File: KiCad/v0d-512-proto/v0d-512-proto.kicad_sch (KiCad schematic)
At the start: 19 parts, among them U1 SST39SF040, U2 62256/628128, U3 74HC139, U4 74HC191, U5 74HC4520, U6 74HC191, U7 74HC191, U8 74HC670

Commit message: fix issues
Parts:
- added JP2, JP3, JP4, JP5: SolderJumper_2_Open, Jumper:SolderJumper-2_P1.3mm_Open_Pad1.0x1.5mm, symbol Jumper:SolderJumper_2_Open
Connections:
- net GND: no longer U6.5 (D/U), U7.5 (D/U)
- net VCC: now also JP1.3 (B), U6.5 (D/U), U7.5 (D/U)
- net pA11: now also JP2.2 (B)
- net pA12: now also JP3.2 (B)
- net pA13: now also JP4.2 (B), JP5.2 (B); no longer JP1.3 (B)
- net pBank0: now also JP2.1 (A)
- net pBank1: now also JP3.1 (A)
- net pBank2: now also JP4.1 (A)
- net pBank3: now also JP5.1 (A)
- net rfAUDIO: no longer names the net of H1.45 (cAUDIO), H1.46 (rfAUDIO)
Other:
- note added: "* 2048KiB PRG FLASH (rewrittable), 32KiB Window * 32KiB PRG RAM, 8KiB Window * 8KiB,32KiB,8KiB CHR RAM, 4x2KiB Window * Four-Screen Scrolling * Scanline IRQ"
- note added: ".... cccc"
- note added: ".... pppp"
- note added: "128K"
- note added: "32K"
- note added: "512K Through-Hole Proto"
- note added: "8K"
- note removed: "* 2048KiB PRG FLASH (rewrittable), 32KiB Window * 32KiB PRG RAM, 8KiB Window * 32KiB CHR RAM, 4x4KiB Window * Four-Screen Scrolling * Scanline IRQ"
- note removed: ".... bbbb"
- note removed: "is.. bbbb"
- moved on the sheet: H1, JP1, RN1, U1, U2, U3A, U3B, U4, U5A, U5B, U6, U7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

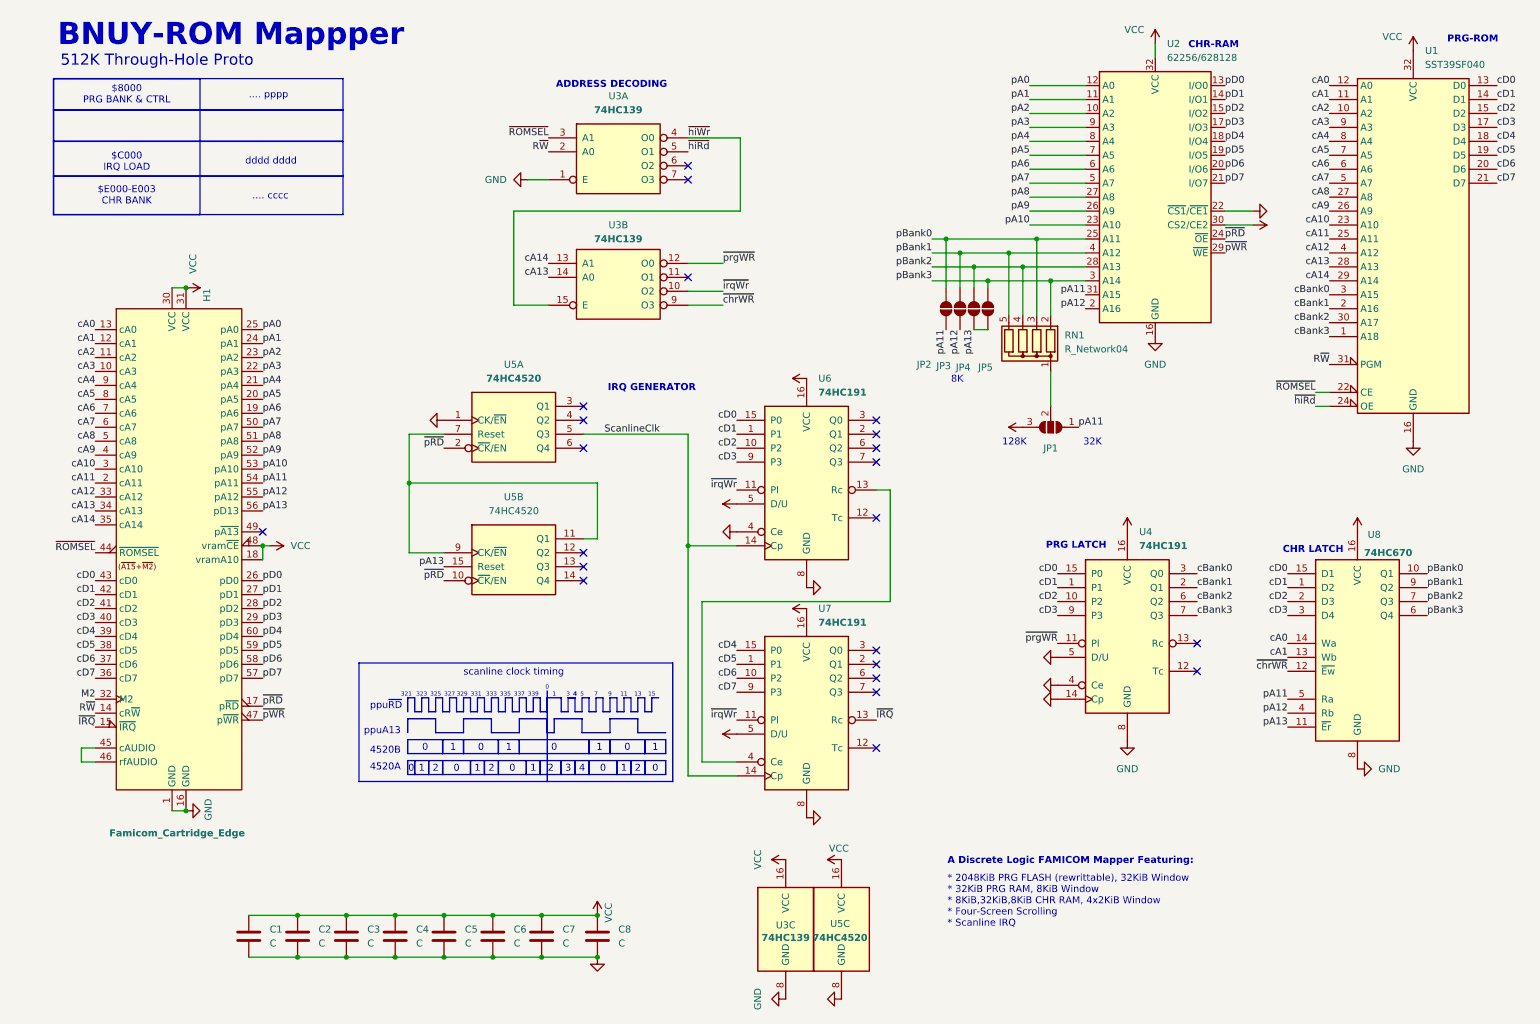
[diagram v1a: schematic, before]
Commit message: Update to latest pcb version, README tweaks
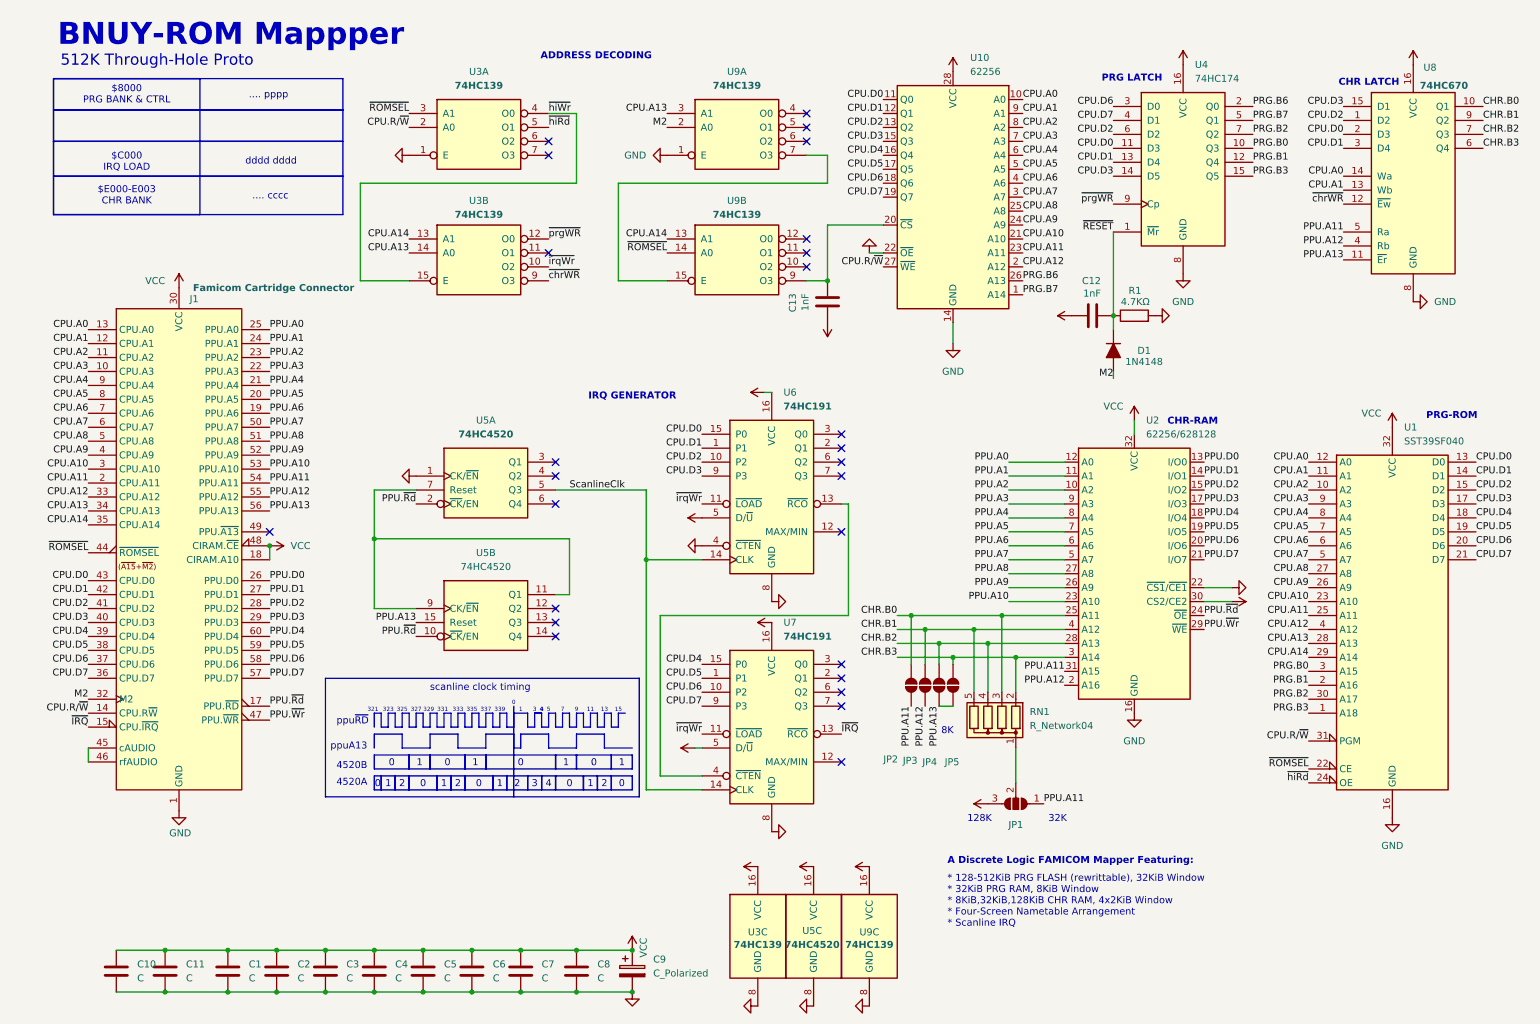
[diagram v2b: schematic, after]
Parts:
- removed U4: 74HC191, Package_DIP:DIP-16_W7.62mm, symbol 74xx:74LS191
- added C10, C11: C, Capacitor_THT:C_Disc_D3.0mm_W1.6mm_P2.50mm, symbol Device:C
- added C12, C13: 1nF, Capacitor_THT:C_Disc_D3.0mm_W1.6mm_P2.50mm, symbol Device:C
- added C9: C_Polarized, Capacitor_THT:CP_Radial_D5.0mm_P2.50mm, symbol Device:C_Polarized
- added D1: 1N4148, PCM_Diode_THT_AKL:D_DO-35_SOD27_P2.54mm_Vertical_AnodeUp, symbol PCM_Diode_AKL:1N4148
- added R1: 4.7KΩ, Resistor_THT:R_Axial_DIN0204_L3.6mm_D1.6mm_P2.54mm_Vertical, symbol Device:R
- added U10: 62256, Package_DIP:DIP-28_W15.24mm, symbol Memory_RAM:CY62256-70PC
- added U4: 74HC174, Package_DIP:DIP-16_W7.62mm, symbol 74xx:74LS174
- added U9: 74HC139, Package_DIP:DIP-16_W7.62mm, symbol 74xx:74LS139
- J1: renamed from H1; value Famicom_Cartridge_Edge -> Famicom Cartridge Connector
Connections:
- net GND: now also C10.2, C11.2, C9.2, R1.2, U10.14 (GND), U10.22 (~{OE}), U4.8 (GND), U9.1 (E), U9.8 (GND)
- net M2: now also D1.2 (A), U9.2 (A0)
- net VCC: now also C10.1, C11.1, C12.1, C13.1, C9.1, U10.28 (VCC), U4.16 (VCC), U9.16 (VCC)
- net ~{ROMSEL}: now also U9.14 (A0)
- net ~{prgWR}: now also U4.9 (Cp)
- net R~{W} renamed CPU.R/~{W}
- net CPU.R/~{W}: now also U10.27 (~{WE})
- net cA0 renamed CPU.A0
- net CPU.A0: now also U10.10 (A0)
- net cA1 renamed CPU.A1
- net CPU.A1: now also U10.9 (A1)
- net cA10 renamed CPU.A10
- net CPU.A10: now also U10.21 (A10)
- net cA11 renamed CPU.A11
- net CPU.A11: now also U10.23 (A11)
- net cA12 renamed CPU.A12
- net CPU.A12: now also U10.2 (A12)
- net cA13 renamed CPU.A13
- net CPU.A13: now also U9.3 (A1)
- net cA14 renamed CPU.A14
- net CPU.A14: now also U9.13 (A1)
- net cA2 renamed CPU.A2
- net CPU.A2: now also U10.8 (A2)
- net cA3 renamed CPU.A3
- net CPU.A3: now also U10.7 (A3)
- net cA4 renamed CPU.A4
- net CPU.A4: now also U10.6 (A4)
- net cA5 renamed CPU.A5
- net CPU.A5: now also U10.5 (A5)
- net cA6 renamed CPU.A6
- net CPU.A6: now also U10.4 (A6)
- net cA7 renamed CPU.A7
- net CPU.A7: now also U10.3 (A7)
- net cA8 renamed CPU.A8
- net CPU.A8: now also U10.25 (A8)
- net cA9 renamed CPU.A9
- net CPU.A9: now also U10.24 (A9)
- net cBank0 renamed PRG.B0
- net PRG.B0: now also U4.10 (Q3)
- net cBank1 renamed PRG.B1
- net PRG.B1: now also U4.12 (Q4)
- net cBank2 renamed PRG.B2
- net PRG.B2: now also U4.7 (Q2)
- net cBank3 renamed PRG.B3
- net PRG.B3: now also U4.15 (Q5)
- net cD0 renamed CPU.D0
- net CPU.D0: now also U8.2 (D3), U10.11 (Q0), U4.11 (D3); no longer U8.15 (D1)
- net cD1 renamed CPU.D1
- net CPU.D1: now also U8.3 (D4), U10.12 (Q1), U4.13 (D4); no longer U8.1 (D2)
- net cD2 renamed CPU.D2
- net CPU.D2: now also U8.1 (D2), U10.13 (Q2), U4.6 (D2); no longer U8.2 (D3)
- net cD3 renamed CPU.D3
- net CPU.D3: now also U8.15 (D1), U10.15 (Q3), U4.14 (D5); no longer U8.3 (D4)
- net cD4 renamed CPU.D4
- net CPU.D4: now also U10.16 (Q4)
- net cD5 renamed CPU.D5
- net CPU.D5: now also U10.17 (Q5)
- net cD6 renamed CPU.D6
- net CPU.D6: now also U10.18 (Q6), U4.3 (D0)
- net cD7 renamed CPU.D7
- net CPU.D7: now also U10.19 (Q7), U4.4 (D1)
- net pA0 renamed PPU.A0
- net pA1 renamed PPU.A1
- net pA10 renamed PPU.A10
- net pA11 renamed PPU.A11
- net pA12 renamed PPU.A12
- net pA13 renamed PPU.A13
- net pA2 renamed PPU.A2
- net pA3 renamed PPU.A3
- net pA4 renamed PPU.A4
- net pA5 renamed PPU.A5
- net pA6 renamed PPU.A6
- net pA7 renamed PPU.A7
- net pA8 renamed PPU.A8
- net pA9 renamed PPU.A9
- net pBank0 renamed CHR.B0
- net pBank1 renamed CHR.B1
- net pBank2 renamed CHR.B2
- net pBank3 renamed CHR.B3
- net pD0 renamed PPU.D0
- net pD1 renamed PPU.D1
- net pD2 renamed PPU.D2
- net pD3 renamed PPU.D3
- net pD4 renamed PPU.D4
- net pD5 renamed PPU.D5
- net pD6 renamed PPU.D6
- net pD7 renamed PPU.D7
- net ~{pRD} renamed PPU.~{Rd}
- net ~{pWR} renamed PPU.~{Wr}
- new net: C13.2, U10.20 (~{CS}), U9.9 (O3)
- new net: U9.15 (E), U9.7 (O3)
- new net PRG.B6: U10.26 (A13), U4.2 (Q0)
- new net PRG.B7: U10.1 (A14), U4.5 (Q1)
- new net ~{RESET}: C12.2, D1.1 (K), R1.1, U4.1 (~{Mr})
- no-connect marks 22 -> 26
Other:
- note added: "* 128-512KiB PRG FLASH (rewrittable), 32KiB Window * 32KiB PRG RAM, 8KiB Window * 8KiB,32KiB,128KiB CHR RAM, 4x2KiB Window * Four-Screen Nametable Arrangement * Scanline IRQ"
- note removed: "* 2048KiB PRG FLASH (rewrittable), 32KiB Window * 32KiB PRG RAM, 8KiB Window * 8KiB,32KiB,8KiB CHR RAM, 4x2KiB Window * Four-Screen Scrolling * Scanline IRQ"
- moved on the sheet: C1, C2, C3, C4, C5, C6, C7, C8, JP1, JP2, JP3, JP4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
